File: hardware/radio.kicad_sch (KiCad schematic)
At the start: 64 parts, among them J1 105450-0101, J2 Conn_01x02, J3 Conn_01x02, J4 Conn_01x04, J5 Conn_01x02_Male, Q1 Q_PMOS_DGS, Q2 Q_NMOS_DGS, Q3 Q_NMOS_DGS, Q4 Q_PMOS_DGS, SW1 SW_BOOT, SW2 SW_RST, SW3 SW_1, SW4 Rot_Enc, SW5 SW_2, SW6 SW_3, U1 TP4056, U2 ESP32-WROOM-32, U3 TPS5432, U4 MAX98357

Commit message: redone DC-DC converter layout to match the reference in datasheet
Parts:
- L1: footprint wyswietlacze:L_2010Metric -> wyswietlacze:DJNR6028-2R2-S; Sklep https://www.mouser.pl/ProductDetail/Bourns/SRP2010TMA-2R2M?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 -> https://www.tme.eu/pl/details/djnr6028-2r2-s/dlawiki-smd-mo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
- TP1, TP2: footprint (none) -> TestPoint:TestPoint_Loop_D2.50mm_Drill1.0mm
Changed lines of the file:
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@@
       (effects (font (size 1.27 1.27)) (justify left))
     )
-    (property "Footprint" "" (id 2) (at 156.21 186.69 0)
+    (property "Footprint" "TestPoint:TestPoint_Loop_D2.50mm_Drill1.0mm" (id 2) (at 156.21 186.69 0)
       (effects (font (size 1.27 1.27)) hide)
     )
@@
     (property "Reference" "L1" (id 0) (at 228.6 22.86 90))
     (property "Value" "2.2u" (id 1) (at 228.6 25.4 90))
-    (property "Footprint" "wyswietlacze:L_2010Metric" (id 2) (at 228.6 29.21 0)
+    (property "Footprint" "wyswietlacze:DJNR6028-2R2-S" (id 2) (at 228.6 29.21 0)
       (effects (font (size 1.27 1.27)) hide)
     )
@@
       (effects (font (size 1.27 1.27)) hide)
     )
-    (property "Sklep" "https://www.mouser.pl/ProductDetail/Bourns/SRP2010TMA-2R2M?qs=sGAEpiMZZMv126LJFLh8yyP1h6mULV5nk26puzcRhPw%3D" (id 5) (at 228.6 29.21 90)
+    (property "Sklep" "https://www.tme.eu/pl/details/djnr6028-2r2-s/dlawiki-smd-mocy/ferrocore/" (id 5) (at 228.6 29.21 90)
       (effects (font (size 1.27 1.27)) hide)
     )
@@
       (effects (font (size 1.27 1.27)) (justify left))
     )
-    (property "Footprint" "" (id 2) (at 170.18 186.69 0)
+    (property "Footprint" "TestPoint:TestPoint_Loop_D2.50mm_Drill1.0mm" (id 2) (at 170.18 186.69 0)
       (effects (font (size 1.27 1.27)) hide)
     )
@@
   (symbol (lib_id "power:GND") (at 158.75 191.77 0) (unit 1)
     (in_bom yes) (on_board yes) (fields_autoplaced)
-    (property "Reference" "#PWR?" (id 0) (at 158.75 198.12 0)
+    (property "Reference" "#PWR0115" (id 0) (at 158.75 198.12 0)
       (effects (font (size 1.27 1.27)) hide)
     )
@@
       (reference "#PWR0114") (unit 1) (value "+3V3") (footprint "")
     )
+    (path "/f73179c7-64e4-4f62-9c58-7c3400f3435c"
+      (reference "#PWR0115") (unit 1) (value "GND") (footprint "")
+    )
     (path "/ec09260e-946a-4d95-8812-f92989b6ac9f"
       (reference "#PWR0116") (unit 1) (value "+5V") (footprint "")
@@
       (reference "#PWR0124") (unit 1) (value "+3V3") (footprint "")
     )
-    (path "/f73179c7-64e4-4f62-9c58-7c3400f3435c"
-      (reference "#PWR?") (unit 1) (value "GND") (footprint "")
-    )
     (path "/31276b67-1ce3-42d3-a55d-ef9419463436"
       (reference "C1") (unit 1) (value "10u") (footprint "Capacitor_SMD:C_1206_3216Metric")
@@
     )
     (path "/6eb0ce94-6235-4154-a551-0d7ecb6dedfa"
-      (reference "L1") (unit 1) (value "2.2u") (footprint "wyswietlacze:L_2010Metric")
+      (reference "L1") (unit 1) (value "2.2u") (footprint "wyswietlacze:DJNR6028-2R2-S")
     )
     (path "/6b5ab209-e7a1-41de-b505-26afad5fe72f"
@@
     )
     (path "/25c71baa-00a8-4ec2-be04-656a7bf9cecb"
-      (reference "TP1") (unit 1) (value "TestPoint") (footprint "")
+      (reference "TP1") (unit 1) (value "TestPoint") (footprint "TestPoint:TestPoint_Loop_D2.50mm_Drill1.0mm")
     )
     (path "/e9301eb0-4603-469f-9fe6-01969d48b33c"
-      (reference "TP2") (unit 1) (value "TestPoint") (footprint "")
+      (reference "TP2") (unit 1) (value "TestPoint") (footprint "TestPoint:TestPoint_Loop_D2.50mm_Drill1.0mm")
     )
     (path "/a274958a-ae53-4989-b48b-9f41b3964f32"

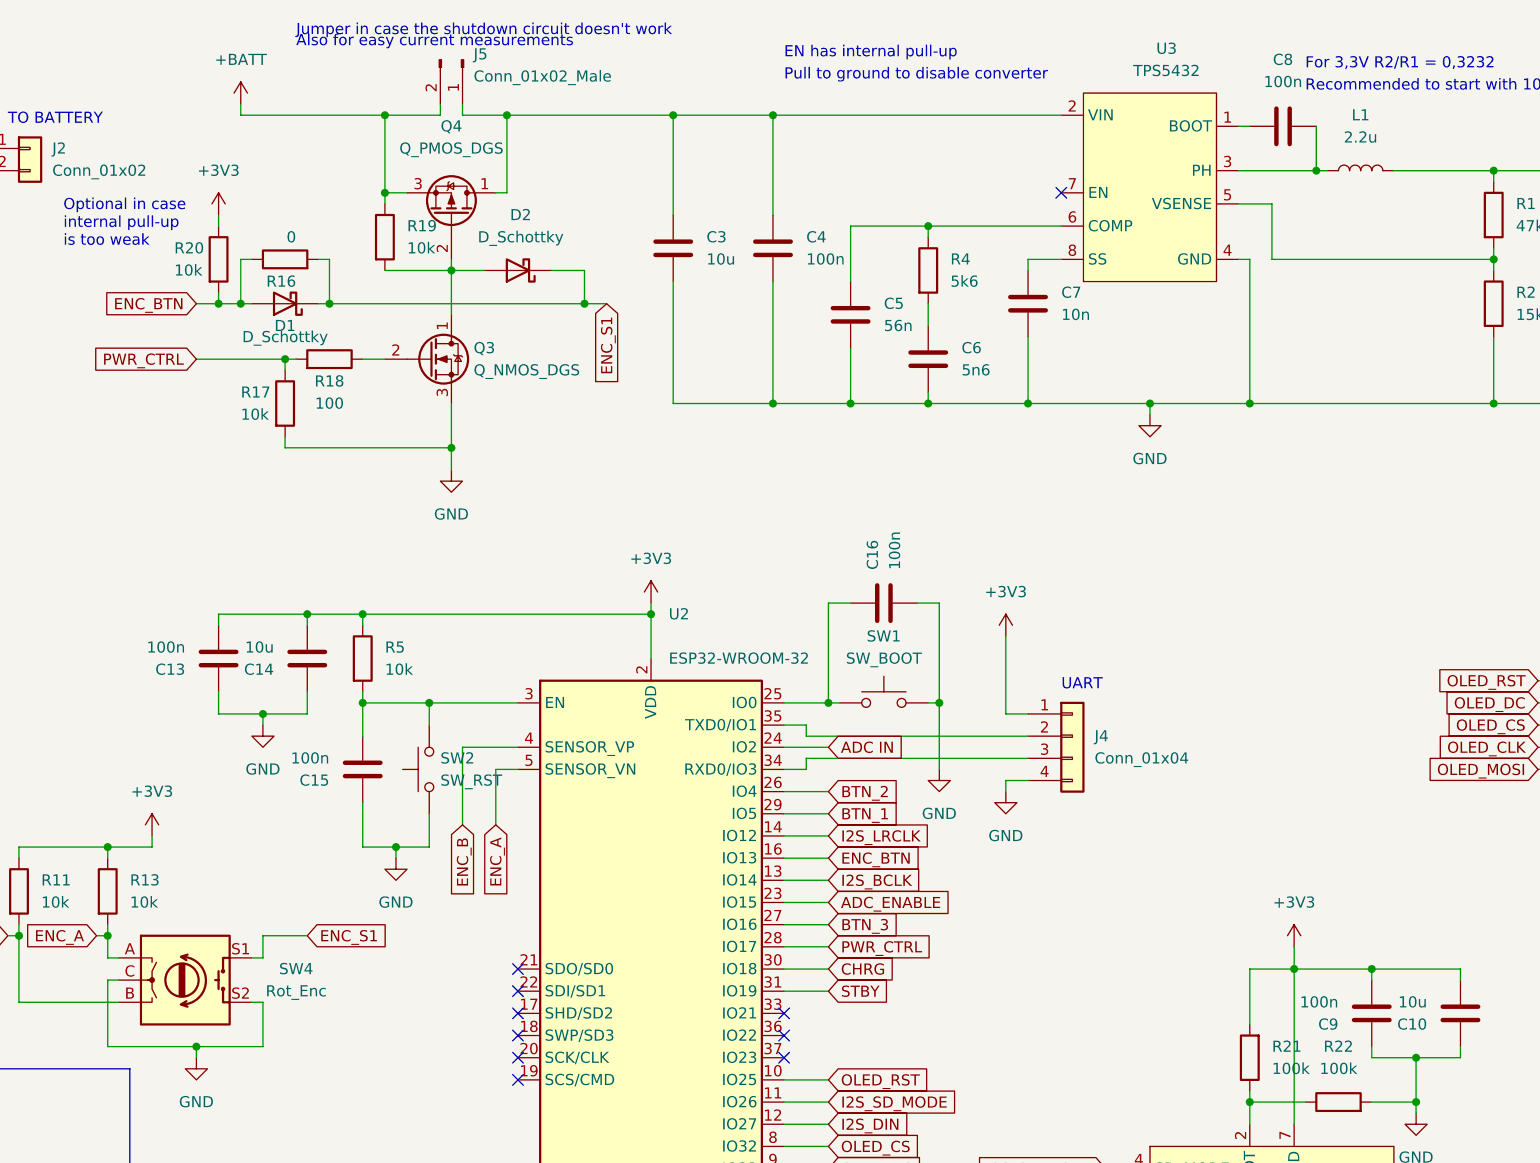
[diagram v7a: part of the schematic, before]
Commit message: removed irrelevant jumper (J5) comment
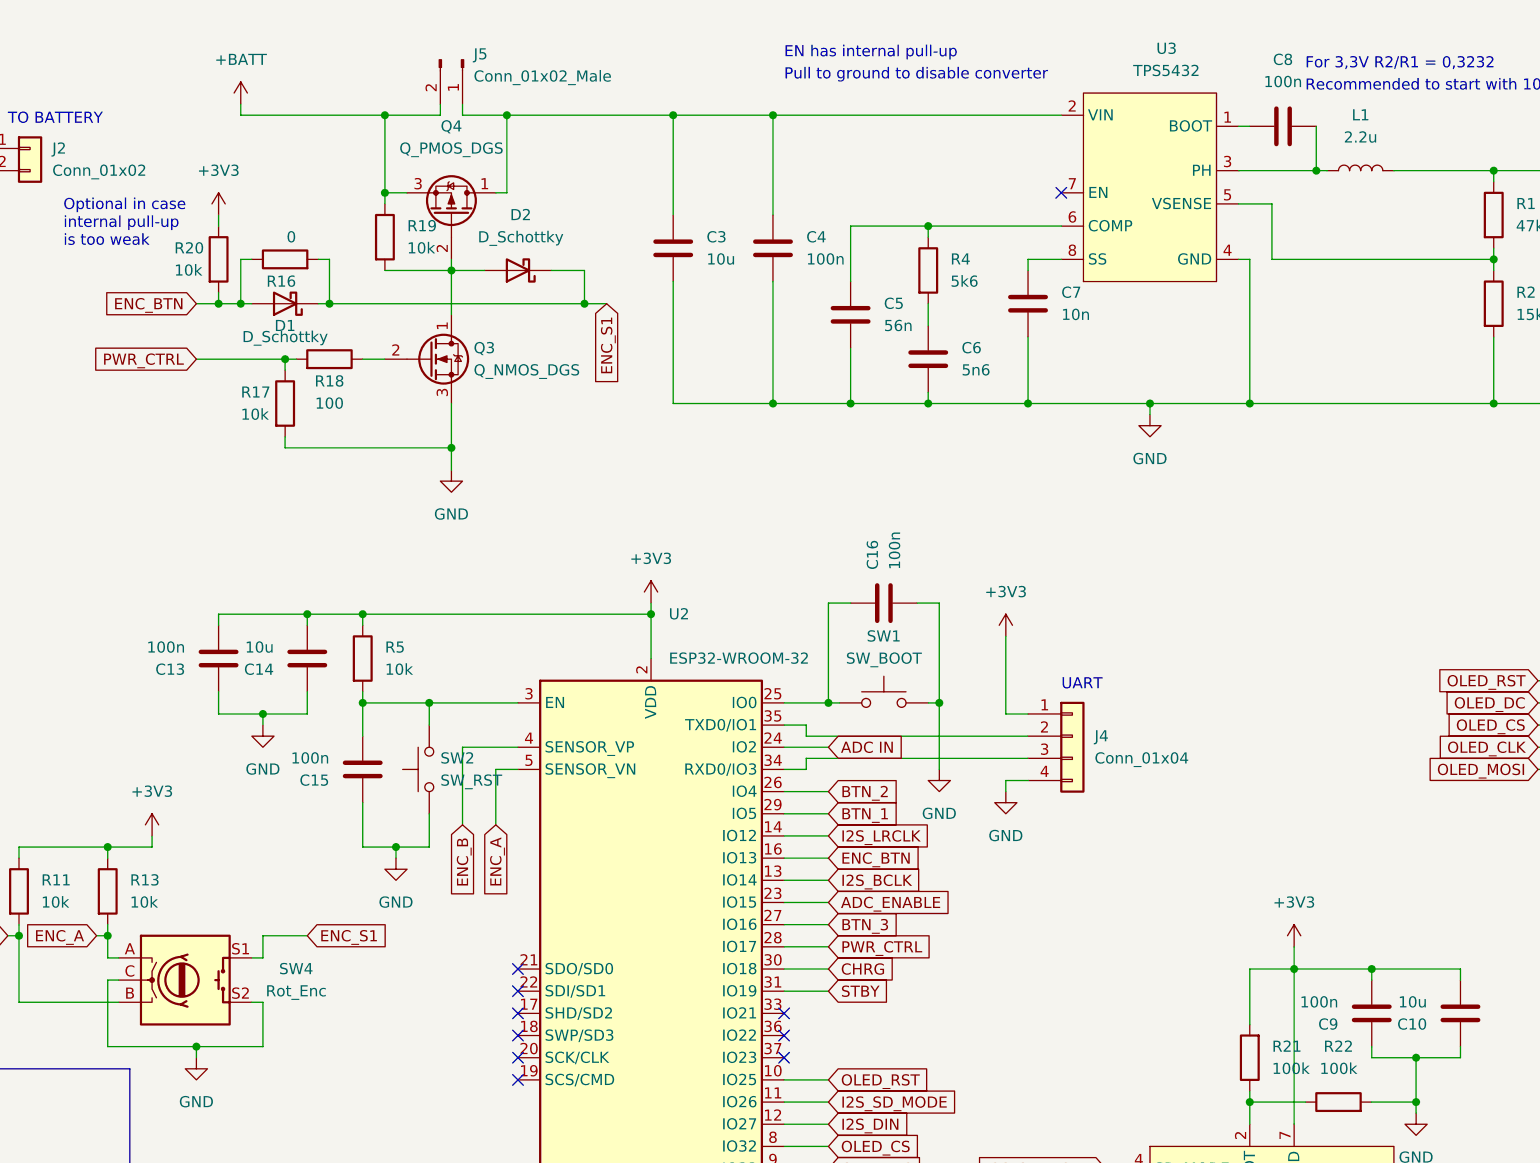
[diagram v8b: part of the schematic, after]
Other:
- note removed: "Also for easy current measurements"
- note removed: "Jumper in case the shutdown circuit doesn't work"
